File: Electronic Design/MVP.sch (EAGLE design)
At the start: 36 parts, among them IC1 ACS712ELC-5A, IC2 ATMEGA328-PU, Q1 IRF9540, Q2 IRF9540, X1 16MHz

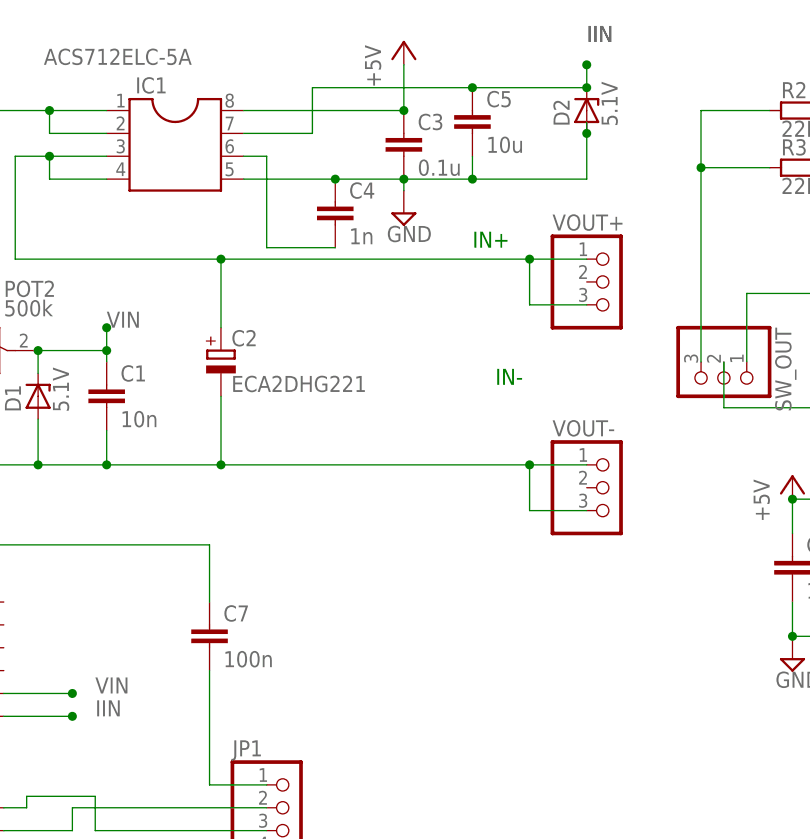
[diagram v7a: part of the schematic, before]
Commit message: changing all caps and resistors to correct size
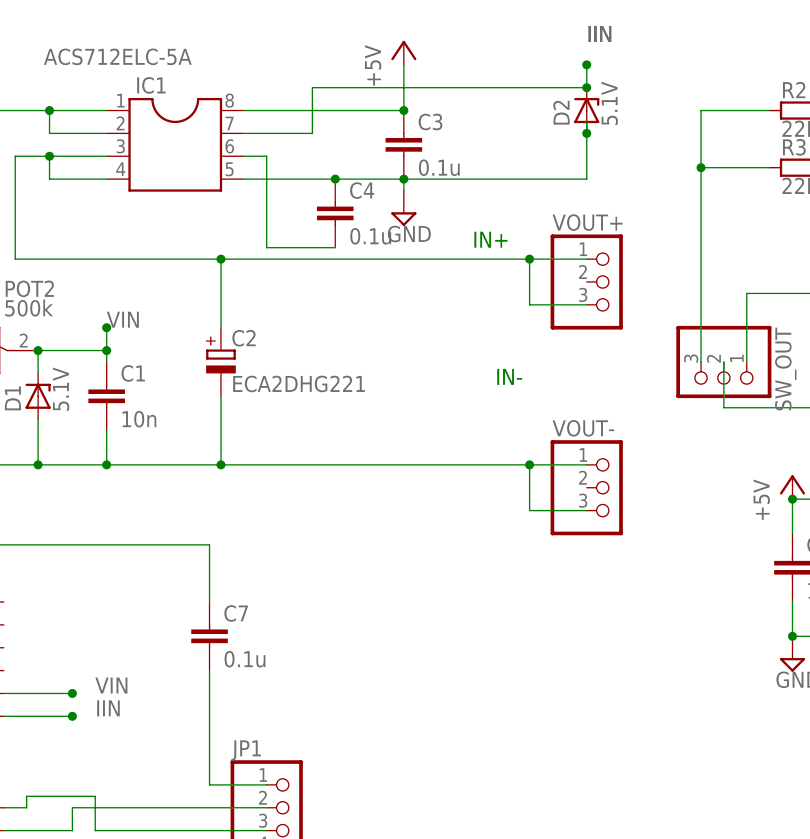
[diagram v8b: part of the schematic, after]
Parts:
- removed C5: 10u, resistor:C-EUC1210
- C1, C3, C6: device resistor:C-EUC1210 -> resistor:C-EUC1206K
- C4: value 1n -> 0.1u; device resistor:C-EUC1210 -> resistor:C-EUC1206K
- C7: value 100n -> 0.1u; device resistor:C-EUC1210 -> resistor:C-EUC1206K
- C8, C9: device resistor:C-EUC1210 -> resistor:C-EUC0805K
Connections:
- net GND: no longer C5.2
- net IIN: no longer C5.1
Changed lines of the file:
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@@
 <parts>
 <part name="B1" library="rectifier" deviceset="GBPC6" device="" value="GBPC3506W"/>
-<part name="C1" library="resistor" deviceset="C-EU" device="C1210" value="10n"/>
+<part name="C1" library="resistor" deviceset="C-EU" device="C1206K" value="10n"/>
 <part name="C2" library="resistor" deviceset="CPOL-EU" device="E3.5-10" value="ECA2DHG221"/>
 <part name="IC1" library="mylibrary" deviceset="SOIC8" device="" value="ACS712ELC-5A"/>
-<part name="C3" library="resistor" deviceset="C-EU" device="C1210" value="0.1u"/>
+<part name="C3" library="resistor" deviceset="C-EU" device="C1206K" value="0.1u"/>
 <part name="SUPPLY1" library="supply2" deviceset="GND" device=""/>
 <part name="POT2" library="resistor" deviceset="R-TRIMM" device="3296W" value="500k"/>
@@
 <part name="R4" library="resistor" deviceset="R-EU_" device="R1206" value="10k"/>
 <part name="+5V1" library="supply1" deviceset="+5V" device=""/>
-<part name="C7" library="resistor" deviceset="C-EU" device="C1210" value="100n"/>
-<part name="C9" library="resistor" deviceset="C-EU" device="C1210" value="22n"/>
-<part name="C8" library="resistor" deviceset="C-EU" device="C1210" value="22n"/>
+<part name="C7" library="resistor" deviceset="C-EU" device="C1206K" value="0.1u"/>
+<part name="C9" library="resistor" deviceset="C-EU" device="C0805K" value="22n"/>
+<part name="C8" library="resistor" deviceset="C-EU" device="C0805K" value="22n"/>
 <part name="SUPPLY14" library="supply2" deviceset="GND" device=""/>
 <part name="SUPPLY17" library="supply2" deviceset="GND" device=""/>
@@
 <part name="JP1" library="pinhead" deviceset="PINHD-1X6" device=""/>
 <part name="SUPPLY6" library="supply2" deviceset="GND" device=""/>
-<part name="C6" library="resistor" deviceset="C-EU" device="C1210" value="10u"/>
+<part name="C6" library="resistor" deviceset="C-EU" device="C1206K" value="10u"/>
 <part name="VIN_BUCK/BOOST" library="pinhead" deviceset="PINHD-1X3" device=""/>
 <part name="R2" library="resistor-power" deviceset="R" device="RWM8X45" value="22R"/>
@@
 <part name="POT1" library="resistor" deviceset="R-TRIMM" device="3296W" value="500k"/>
 <part name="D1" library="diode" deviceset="ZPD" device="" value="5.1V"/>
-<part name="C5" library="resistor" deviceset="C-EU" device="C1210" value="10u"/>
-<part name="C4" library="resistor" deviceset="C-EU" device="C1210" value="1n"/>
+<part name="C4" library="resistor" deviceset="C-EU" device="C1206K" value="0.1u"/>
 <part name="SW_OUT" library="pinhead" deviceset="PINHD-1X3" device=""/>
 </parts>
@@
 </instance>
 <instance part="D1" gate="G$1" x="-8.89" y="73.66" rot="R90"/>
-<instance part="C5" gate="G$1" x="39.37" y="105.41"/>
 <instance part="C4" gate="G$1" x="24.13" y="95.25"/>
 <instance part="SW_OUT" gate="A" x="67.31" y="74.93" rot="R270"/>
@@
 <segment>
 <wire x1="21.59" y1="102.87" x2="21.59" y2="107.95" width="0.1524" layer="91"/>
-<wire x1="21.59" y1="107.95" x2="39.37" y2="107.95" width="0.1524" layer="91"/>
+<wire x1="21.59" y1="107.95" x2="52.07" y2="107.95" width="0.1524" layer="91"/>
 <pinref part="D2" gate="G$1" pin="C"/>
-<wire x1="39.37" y1="107.95" x2="52.07" y2="107.95" width="0.1524" layer="91"/>
 <wire x1="52.07" y1="107.95" x2="52.07" y2="110.49" width="0.1524" layer="91"/>
 <junction x="52.07" y="110.49"/>
@@
 <pinref part="IC1" gate="G$1" pin="7"/>
 <wire x1="21.59" y1="102.87" x2="13.97" y2="102.87" width="0.1524" layer="91"/>
-<pinref part="C5" gate="G$1" pin="1"/>
-<junction x="39.37" y="107.95"/>
 </segment>
 <segment>
@@
 <pinref part="SUPPLY1" gate="GND" pin="GND"/>
 <junction x="31.75" y="97.79"/>
-<wire x1="39.37" y1="100.33" x2="39.37" y2="97.79" width="0.1524" layer="91"/>
-<wire x1="39.37" y1="97.79" x2="31.75" y2="97.79" width="0.1524" layer="91"/>
-<wire x1="39.37" y1="97.79" x2="52.07" y2="97.79" width="0.1524" layer="91"/>
+<wire x1="31.75" y1="97.79" x2="52.07" y2="97.79" width="0.1524" layer="91"/>
 <wire x1="52.07" y1="97.79" x2="52.07" y2="102.87" width="0.1524" layer="91"/>
 <pinref part="D2" gate="G$1" pin="A"/>
 <wire x1="52.07" y1="102.87" x2="52.07" y2="104.14" width="0.1524" layer="91"/>
 <junction x="52.07" y="102.87"/>
-<junction x="39.37" y="97.79"/>
 <pinref part="IC1" gate="G$1" pin="5"/>
 <wire x1="13.97" y1="97.79" x2="24.13" y2="97.79" width="0.1524" layer="91"/>
 <wire x1="24.13" y1="97.79" x2="31.75" y2="97.79" width="0.1524" layer="91"/>
 <wire x1="31.75" y1="97.79" x2="31.75" y2="96.52" width="0.1524" layer="91"/>
-<pinref part="C5" gate="G$1" pin="2"/>
 <pinref part="C4" gate="G$1" pin="1"/>
 <junction x="24.13" y="97.79"/>
